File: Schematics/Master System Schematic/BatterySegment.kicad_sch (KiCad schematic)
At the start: 148 parts

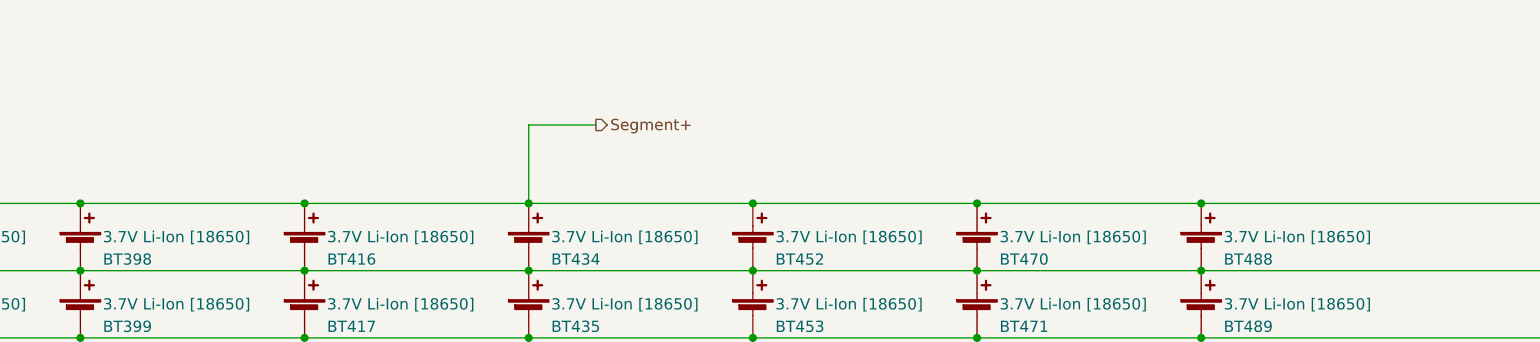
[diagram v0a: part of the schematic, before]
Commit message: Hubert and raajas color coding (#129)
* Charger Wiring Color Code and Wiring Update

Color Coded Wires. Updated wire gauges, added fans and CAN resistor

* Update to accumulator and charger

Update to accumulator and charger color coding

* Master schematic colour coded

* Added 2AWG to colour coding legend

* Update color coding

Update color coding accumulator stuff

* Added wire colours next to legend

* Update for color coding

Update for color coding

* update color and add fan

update color and add fan

* further update

further update

* more update

* more update

more update

* change again

change again

Co-authored-by: Raajas <52158581+Litmusblox@users.noreply.github.com>
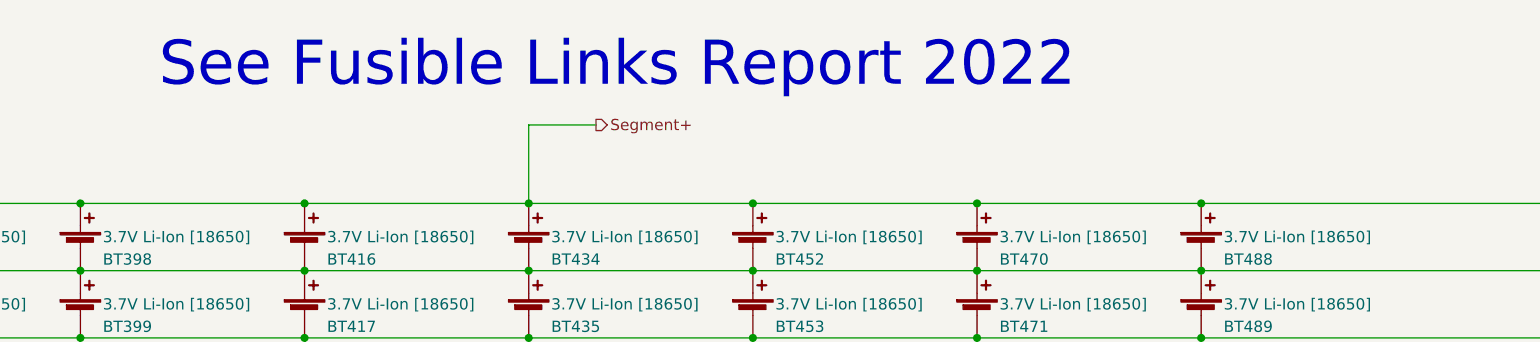
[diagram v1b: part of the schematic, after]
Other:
- note added: "See Fusible Links Report 2022"
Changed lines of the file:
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@@
     (effects (font (size 1.27 1.27)) (justify left bottom))
+  )
+  (text "See Fusible Links Report 2022" (at 102.87 24.13 0)
+    (effects (font (size 5 5)) (justify left bottom))
   )
   (text "*Thermistors are distributed evenly throughout the segment. Each group of 5 has a common ground on the thermistor expansion."

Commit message: ESF-2 2023 Updates (#136)
* Moved shutdown loop & TSMPs

* Moved Dashboard/Footwellbox

* Deleted SSOKs

* More stuff

* Charger and battbox stuff

* Added battbox fans

* Updated sheet sizing

* Flipped MC

 to make powertrain ordering better

* Updated HV plate

* IDrk

* Better topsheet labels

* Segment Layer updates

Adding shepherd

* LV Plate update

* Partial work on accumulator container sheet

To be continued

* Finish accumulator

* Footwell updates

* Removing old files

* Added Wheel

* Top sheet budge

* Renumbered pages

* Shutdown Summary Updates

* Missed some TSV color

* Export shutdown summary

* Deleted more old files

* Added TSAL17

* Added TS-GLV17

* Added Wheel17

* Other NER lib cleanup

* Annotations

* More annotate and export

* Moved PDF

* Reexport master schem

* Cleaning out old shutdown summary files

* MATLAB!

For precharge and discharge plotting

* Changed label alignment

* Updated dashboard name

* Updated for LFP board and bigger top sheet

* backup

* Changed breaker to fuse in Shutdown Simmary

* Finished traces

* Oops forgot to merge
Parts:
- renumbered BT380 to BT1479, BT381 to BT1480, BT382 to BT1481, BT383 to BT1482, BT384 to BT1483, BT385 to BT1484, BT386 to BT1485, BT387 to BT1486, BT388 to BT1487, BT389 to BT1488, BT390 to BT1489, BT391 to BT1490, BT392 to BT1491, BT393 to BT1492, BT394 to BT1493, BT395 to BT1494, BT396 to BT1495, BT397 to BT1496, BT398 to BT1497, BT399 to BT1498, BT400 to BT1499, BT401 to BT1500, BT402 to BT1501, BT403 to BT1502, BT404 to BT1503, BT405 to BT1504, BT406 to BT1505, BT407 to BT1506, BT408 to BT1507, BT409 to BT1508, BT410 to BT1509, BT411 to BT1510, BT412 to BT1511, BT413 to BT1512, BT414 to BT1513, BT415 to BT1514, BT416 to BT1515, BT417 to BT1516, BT418 to BT1517, BT419 to BT1518, BT420 to BT1519, BT421 to BT1520, BT422 to BT1521, BT423 to BT1522, BT424 to BT1523, BT425 to BT1524, BT426 to BT1525, BT427 to BT1526, BT428 to BT1527, BT429 to BT1528, BT430 to BT1529, BT431 to BT1530, BT432 to BT1531, BT433 to BT1532, BT434 to BT1533, BT435 to BT1534, BT436 to BT1535, BT437 to BT1536, BT438 to BT1537, BT439 to BT1538, BT440 to BT1539, BT441 to BT1540, BT442 to BT1541, BT443 to BT1542, BT444 to BT1543, BT445 to BT1544, BT446 to BT1545, BT447 to BT1546, BT448 to BT1547, BT449 to BT1548, BT450 to BT1549, BT451 to BT1550, BT452 to BT1551, BT453 to BT1552, BT454 to BT1553, BT455 to BT1554, BT456 to BT1555, BT457 to BT1556, BT458 to BT1557, BT459 to BT1558, BT460 to BT1559, BT461 to BT1560, BT462 to BT1561, BT463 to BT1562, BT464 to BT1563, BT465 to BT1564, BT466 to BT1565, BT467 to BT1566, BT468 to BT1567, BT469 to BT1568, BT470 to BT1569, BT471 to BT1570, BT472 to BT1571, BT473 to BT1572, BT474 to BT1573, BT475 to BT1574, BT476 to BT1575, BT477 to BT1576, BT478 to BT1577, BT479 to BT1578, BT480 to BT1579, BT481 to BT1580, BT482 to BT1581, BT483 to BT1582, BT484 to BT1583, BT485 to BT1584, BT486 to BT1585, BT487 to BT1586, BT488 to BT1587, BT489 to BT1588, BT490 to BT1589, BT491 to BT1590, BT492 to BT1591, BT493 to BT1592, BT494 to BT1593, BT495 to BT1594, BT496 to BT1595, BT497 to BT1596, BT498 to BT1597, BT499 to BT1598, BT500 to BT1599, BT501 to BT1600, BT502 to BT1601, BT503 to BT1602, BT504 to BT1603, BT505 to BT1604, TH67 to TH1401, TH68 to TH1402, TH69 to TH1403, TH70 to TH1404, TH71 to TH1405, TH72 to TH1406, TH73 to TH1407, TH74 to TH1408, TH75 to TH1409, TH76 to TH1410, TH77 to TH1411, TH78 to TH1412, TH79 to TH1413, TH80 to TH1414, TH81 to TH1415, TH82 to TH1416, TH83 to TH1417, TH84 to TH1418, TH85 to TH1419, TH86 to TH1420, TH87 to TH1421, TH88 to TH1422

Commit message: Revert "ESF-2 2023 Updates (#136)"
This reverts commit dbac7da28cdaad5f36fde89af32aad76a0b85ea3.
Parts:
- renumbered BT1479 to BT380, BT1480 to BT381, BT1481 to BT382, BT1482 to BT383, BT1483 to BT384, BT1484 to BT385, BT1485 to BT386, BT1486 to BT387, BT1487 to BT388, BT1488 to BT389, BT1489 to BT390, BT1490 to BT391, BT1491 to BT392, BT1492 to BT393, BT1493 to BT394, BT1494 to BT395, BT1495 to BT396, BT1496 to BT397, BT1497 to BT398, BT1498 to BT399, BT1499 to BT400, BT1500 to BT401, BT1501 to BT402, BT1502 to BT403, BT1503 to BT404, BT1504 to BT405, BT1505 to BT406, BT1506 to BT407, BT1507 to BT408, BT1508 to BT409, BT1509 to BT410, BT1510 to BT411, BT1511 to BT412, BT1512 to BT413, BT1513 to BT414, BT1514 to BT415, BT1515 to BT416, BT1516 to BT417, BT1517 to BT418, BT1518 to BT419, BT1519 to BT420, BT1520 to BT421, BT1521 to BT422, BT1522 to BT423, BT1523 to BT424, BT1524 to BT425, BT1525 to BT426, BT1526 to BT427, BT1527 to BT428, BT1528 to BT429, BT1529 to BT430, BT1530 to BT431, BT1531 to BT432, BT1532 to BT433, BT1533 to BT434, BT1534 to BT435, BT1535 to BT436, BT1536 to BT437, BT1537 to BT438, BT1538 to BT439, BT1539 to BT440, BT1540 to BT441, BT1541 to BT442, BT1542 to BT443, BT1543 to BT444, BT1544 to BT445, BT1545 to BT446, BT1546 to BT447, BT1547 to BT448, BT1548 to BT449, BT1549 to BT450, BT1550 to BT451, BT1551 to BT452, BT1552 to BT453, BT1553 to BT454, BT1554 to BT455, BT1555 to BT456, BT1556 to BT457, BT1557 to BT458, BT1558 to BT459, BT1559 to BT460, BT1560 to BT461, BT1561 to BT462, BT1562 to BT463, BT1563 to BT464, BT1564 to BT465, BT1565 to BT466, BT1566 to BT467, BT1567 to BT468, BT1568 to BT469, BT1569 to BT470, BT1570 to BT471, BT1571 to BT472, BT1572 to BT473, BT1573 to BT474, BT1574 to BT475, BT1575 to BT476, BT1576 to BT477, BT1577 to BT478, BT1578 to BT479, BT1579 to BT480, BT1580 to BT481, BT1581 to BT482, BT1582 to BT483, BT1583 to BT484, BT1584 to BT485, BT1585 to BT486, BT1586 to BT487, BT1587 to BT488, BT1588 to BT489, BT1589 to BT490, BT1590 to BT491, BT1591 to BT492, BT1592 to BT493, BT1593 to BT494, BT1594 to BT495, BT1595 to BT496, BT1596 to BT497, BT1597 to BT498, BT1598 to BT499, BT1599 to BT500, BT1600 to BT501, BT1601 to BT502, BT1602 to BT503, BT1603 to BT504, BT1604 to BT505, TH1401 to TH67, TH1402 to TH68, TH1403 to TH69, TH1404 to TH70, TH1405 to TH71, TH1406 to TH72, TH1407 to TH73, TH1408 to TH74, TH1409 to TH75, TH1410 to TH76, TH1411 to TH77, TH1412 to TH78, TH1413 to TH79, TH1414 to TH80, TH1415 to TH81, TH1416 to TH82, TH1417 to TH83, TH1418 to TH84, TH1419 to TH85, TH1420 to TH86, TH1421 to TH87, TH1422 to TH88

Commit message: Moved shutdown loop & TSMPs
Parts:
- renumbered BT380 to BT254, BT381 to BT255, BT382 to BT256, BT383 to BT257, BT384 to BT258, BT385 to BT259, BT386 to BT260, BT387 to BT261, BT388 to BT262, BT389 to BT263, BT390 to BT264, BT391 to BT265, BT392 to BT266, BT393 to BT267, BT394 to BT268, BT395 to BT269, BT396 to BT270, BT397 to BT271, BT398 to BT272, BT399 to BT273, BT400 to BT274, BT401 to BT275, BT402 to BT276, BT403 to BT277, BT404 to BT278, BT405 to BT279, BT406 to BT280, BT407 to BT281, BT408 to BT282, BT409 to BT283, BT410 to BT284, BT411 to BT285, BT412 to BT286, BT413 to BT287, BT414 to BT288, BT415 to BT289, BT416 to BT290, BT417 to BT291, BT418 to BT292, BT419 to BT293, BT420 to BT294, BT421 to BT295, BT422 to BT296, BT423 to BT297, BT424 to BT298, BT425 to BT299, BT426 to BT300, BT427 to BT301, BT428 to BT302, BT429 to BT303, BT430 to BT304, BT431 to BT305, BT432 to BT306, BT433 to BT307, BT434 to BT308, BT435 to BT309, BT436 to BT310, BT437 to BT311, BT438 to BT312, BT439 to BT313, BT440 to BT314, BT441 to BT315, BT442 to BT316, BT443 to BT317, BT444 to BT318, BT445 to BT319, BT446 to BT320, BT447 to BT321, BT448 to BT322, BT449 to BT323, BT450 to BT324, BT451 to BT325, BT452 to BT326, BT453 to BT327, BT454 to BT328, BT455 to BT329, BT456 to BT330, BT457 to BT331, BT458 to BT332, BT459 to BT333, BT460 to BT334, BT461 to BT335, BT462 to BT336, BT463 to BT337, BT464 to BT338, BT465 to BT339, BT466 to BT340, BT467 to BT341, BT468 to BT342, BT469 to BT343, BT470 to BT344, BT471 to BT345, BT472 to BT346, BT473 to BT347, BT474 to BT348, BT475 to BT349, BT476 to BT350, BT477 to BT351, BT478 to BT352, BT479 to BT353, BT480 to BT354, BT481 to BT355, BT482 to BT356, BT483 to BT357, BT484 to BT358, BT485 to BT359, BT486 to BT360, BT487 to BT361, BT488 to BT362, BT489 to BT363, BT490 to BT364, BT491 to BT365, BT492 to BT366, BT493 to BT367, BT494 to BT368, BT495 to BT369, BT496 to BT370, BT497 to BT371, BT498 to BT372, BT499 to BT373, BT500 to BT374, BT501 to BT375, BT502 to BT376, BT503 to BT377, BT504 to BT378, BT505 to BT379, TH67 to TH45, TH68 to TH46, TH69 to TH47, TH70 to TH48, TH71 to TH49, TH72 to TH50, TH73 to TH51, TH74 to TH52, TH75 to TH53, TH76 to TH54, TH77 to TH55, TH78 to TH56, TH79 to TH57, TH80 to TH58, TH81 to TH59, TH82 to TH60, TH83 to TH61, TH84 to TH62, TH85 to TH63, TH86 to TH64, TH87 to TH65, TH88 to TH66

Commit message: more update
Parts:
- renumbered BT254 to BT380, BT255 to BT381, BT256 to BT382, BT257 to BT383, BT258 to BT384, BT259 to BT385, BT260 to BT386, BT261 to BT387, BT262 to BT388, BT263 to BT389, BT264 to BT390, BT265 to BT391, BT266 to BT392, BT267 to BT393, BT268 to BT394, BT269 to BT395, BT270 to BT396, BT271 to BT397, BT272 to BT398, BT273 to BT399, BT274 to BT400, BT275 to BT401, BT276 to BT402, BT277 to BT403, BT278 to BT404, BT279 to BT405, BT280 to BT406, BT281 to BT407, BT282 to BT408, BT283 to BT409, BT284 to BT410, BT285 to BT411, BT286 to BT412, BT287 to BT413, BT288 to BT414, BT289 to BT415, BT290 to BT416, BT291 to BT417, BT292 to BT418, BT293 to BT419, BT294 to BT420, BT295 to BT421, BT296 to BT422, BT297 to BT423, BT298 to BT424, BT299 to BT425, BT300 to BT426, BT301 to BT427, BT302 to BT428, BT303 to BT429, BT304 to BT430, BT305 to BT431, BT306 to BT432, BT307 to BT433, BT308 to BT434, BT309 to BT435, BT310 to BT436, BT311 to BT437, BT312 to BT438, BT313 to BT439, BT314 to BT440, BT315 to BT441, BT316 to BT442, BT317 to BT443, BT318 to BT444, BT319 to BT445, BT320 to BT446, BT321 to BT447, BT322 to BT448, BT323 to BT449, BT324 to BT450, BT325 to BT451, BT326 to BT452, BT327 to BT453, BT328 to BT454, BT329 to BT455, BT330 to BT456, BT331 to BT457, BT332 to BT458, BT333 to BT459, BT334 to BT460, BT335 to BT461, BT336 to BT462, BT337 to BT463, BT338 to BT464, BT339 to BT465, BT340 to BT466, BT341 to BT467, BT342 to BT468, BT343 to BT469, BT344 to BT470, BT345 to BT471, BT346 to BT472, BT347 to BT473, BT348 to BT474, BT349 to BT475, BT350 to BT476, BT351 to BT477, BT352 to BT478, BT353 to BT479, BT354 to BT480, BT355 to BT481, BT356 to BT482, BT357 to BT483, BT358 to BT484, BT359 to BT485, BT360 to BT486, BT361 to BT487, BT362 to BT488, BT363 to BT489, BT364 to BT490, BT365 to BT491, BT366 to BT492, BT367 to BT493, BT368 to BT494, BT369 to BT495, BT370 to BT496, BT371 to BT497, BT372 to BT498, BT373 to BT499, BT374 to BT500, BT375 to BT501, BT376 to BT502, BT377 to BT503, BT378 to BT504, BT379 to BT505, TH45 to TH67, TH46 to TH68, TH47 to TH69, TH48 to TH70, TH49 to TH71, TH50 to TH72, TH51 to TH73, TH52 to TH74, TH53 to TH75, TH54 to TH76, TH55 to TH77, TH56 to TH78, TH57 to TH79, TH58 to TH80, TH59 to TH81, TH60 to TH82, TH61 to TH83, TH62 to TH84, TH63 to TH85, TH64 to TH86, TH65 to TH87, TH66 to TH88
